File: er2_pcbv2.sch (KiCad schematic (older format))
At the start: 39 parts, among them J1 HMC5883L, J2 SPI1, J3 raspberry_b_plus_header, J4 Power, U1 MPU-6050, U2 LM2596S-5, U3 STM32F030K6Tx, Y1 8Mhz

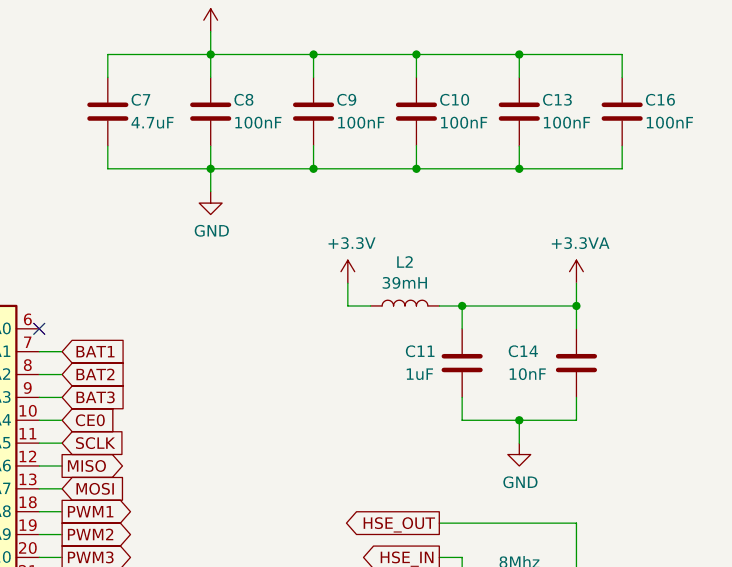
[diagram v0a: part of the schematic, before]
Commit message: packages of PCB components was assigned
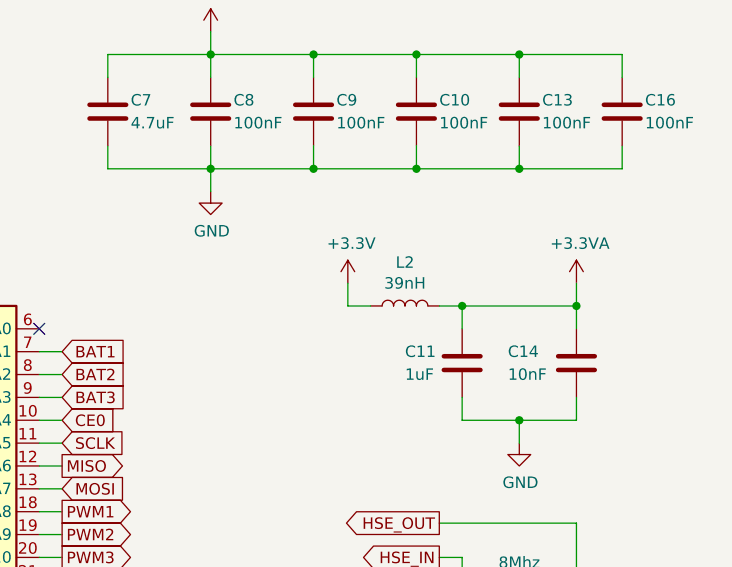
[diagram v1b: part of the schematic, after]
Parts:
- C1, C10, C11, C12, C13, C14, C15, C16, C2, C3, C4, C7, C8, C9: footprint (none) -> Capacitor_SMD:C_0805_2012Metric_Pad1.18x1.45mm_HandSolder
- C5: footprint (none) -> Capacitor_SMD:CP_Elec_10x10.5
- C6: footprint (none) -> Capacitor_SMD:CP_Elec_6.3x7.7
- D1, D3: footprint (none) -> LED_SMD:LED_0805_2012Metric_Pad1.15x1.40mm_HandSolder
- D2: footprint Diode_THT:D_DO-201AD_P15.24mm_Horizontal -> (none)
- J3: footprint (none) -> Connector_PinHeader_2.54mm:PinHeader_2x13_P2.54mm_Vertical
- J4: footprint (none) -> Connector_JST:JST_XH_B4B-XH-A_1x04_P2.50mm_Vertical
- L2: value 39mH -> 39nH
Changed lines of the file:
@@
 F 0 "D1" V 1139 5232 50  0000 R CNN
 F 1 "LED" V 1048 5232 50  0000 R CNN
-F 2 "" H 1100 5350 50  0001 C CNN
+F 2 "LED_SMD:LED_0805_2012Metric_Pad1.15x1.40mm_HandSolder" H 1100 5350 50  0001 C CNN
 F 3 "~" H 1100 5350 50  0001 C CNN
 	1    1100 5350
@@
 F 0 "J3" H 4550 7350 50  0000 C CNN
 F 1 "raspberry_b_plus_header" H 4800 5700 50  0000 C CNN
-F 2 "" H 4300 6450 50  0001 C CNN
+F 2 "Connector_PinHeader_2.54mm:PinHeader_2x13_P2.54mm_Vertical" H 4300 6450 50  0001 C CNN
 F 3 "" H 4300 6450 50  0001 C CNN
 	1    4350 6350
@@
 F 0 "C15" H 10715 5696 50  0000 L CNN
 F 1 "20p" H 10715 5605 50  0000 L CNN
-F 2 "" H 10638 5500 50  0001 C CNN
+F 2 "Capacitor_SMD:C_0805_2012Metric_Pad1.18x1.45mm_HandSolder" H 10638 5500 50  0001 C CNN
 F 3 "~" H 10600 5650 50  0001 C CNN
 	1    10600 5650
@@
 F 0 "C12" H 9850 5700 50  0000 L CNN
 F 1 "20p" H 9850 5600 50  0000 L CNN
-F 2 "" H 10138 5500 50  0001 C CNN
+F 2 "Capacitor_SMD:C_0805_2012Metric_Pad1.18x1.45mm_HandSolder" H 10138 5500 50  0001 C CNN
 F 3 "~" H 10100 5650 50  0001 C CNN
 	1    10100 5650
@@
 F 0 "C1" H 2915 3946 50  0000 L CNN
 F 1 "0.1uF" H 2915 3855 50  0000 L CNN
-F 2 "" H 2838 3750 50  0001 C CNN
+F 2 "Capacitor_SMD:C_0805_2012Metric_Pad1.18x1.45mm_HandSolder" H 2838 3750 50  0001 C CNN
 F 3 "~" H 2800 3900 50  0001 C CNN
 	1    2800 3900
@@
 F 0 "C2" H 3415 3946 50  0000 L CNN
 F 1 "2.2nF" H 3415 3855 50  0000 L CNN
-F 2 "" H 3338 3750 50  0001 C CNN
+F 2 "Capacitor_SMD:C_0805_2012Metric_Pad1.18x1.45mm_HandSolder" H 3338 3750 50  0001 C CNN
 F 3 "~" H 3300 3900 50  0001 C CNN
 	1    3300 3900
@@
 F 0 "C3" H 4100 3450 50  0000 L CNN
 F 1 "10nF" H 4100 3350 50  0000 L CNN
-F 2 "" H 4488 3250 50  0001 C CNN
+F 2 "Capacitor_SMD:C_0805_2012Metric_Pad1.18x1.45mm_HandSolder" H 4488 3250 50  0001 C CNN
 F 3 "~" H 4450 3400 50  0001 C CNN
 	1    4450 3400
@@
 F 0 "C4" H 4915 3446 50  0000 L CNN
 F 1 "0.1uF" H 4915 3355 50  0000 L CNN
-F 2 "" H 4838 3250 50  0001 C CNN
+F 2 "Capacitor_SMD:C_0805_2012Metric_Pad1.18x1.45mm_HandSolder" H 4838 3250 50  0001 C CNN
 F 3 "~" H 4800 3400 50  0001 C CNN
 	1    4800 3400
@@
 F 0 "C11" H 9850 4400 50  0000 L CNN
 F 1 "1uF" H 9850 4300 50  0000 L CNN
-F 2 "" H 10138 4200 50  0001 C CNN
+F 2 "Capacitor_SMD:C_0805_2012Metric_Pad1.18x1.45mm_HandSolder" H 10138 4200 50  0001 C CNN
 F 3 "~" H 10100 4350 50  0001 C CNN
 	1    10100 4350
@@
 F 0 "C14" H 10300 4400 50  0000 L CNN
 F 1 "10nF" H 10300 4300 50  0000 L CNN
-F 2 "" H 10638 4200 50  0001 C CNN
+F 2 "Capacitor_SMD:C_0805_2012Metric_Pad1.18x1.45mm_HandSolder" H 10638 4200 50  0001 C CNN
 F 3 "~" H 10600 4350 50  0001 C CNN
 	1    10600 4350
@@
 P 9850 4100
 F 0 "L2" V 10040 4100 50  0000 C CNN
-F 1 "39mH" V 9949 4100 50  0000 C CNN
+F 1 "39nH" V 9949 4100 50  0000 C CNN
 F 2 "" H 9850 4100 50  0001 C CNN
 F 3 "~" H 9850 4100 50  0001 C CNN
@@
 F 0 "C9" H 9550 3300 50  0000 L CNN
 F 1 "100nF" H 9550 3200 50  0000 L CNN
-F 2 "" H 9488 3100 50  0001 C CNN
+F 2 "Capacitor_SMD:C_0805_2012Metric_Pad1.18x1.45mm_HandSolder" H 9488 3100 50  0001 C CNN
 F 3 "~" H 9450 3250 50  0001 C CNN
 	1    9450 3250
@@
 F 0 "C10" H 10000 3300 50  0000 L CNN
 F 1 "100nF" H 10000 3200 50  0000 L CNN
-F 2 "" H 9938 3100 50  0001 C CNN
+F 2 "Capacitor_SMD:C_0805_2012Metric_Pad1.18x1.45mm_HandSolder" H 9938 3100 50  0001 C CNN
 F 3 "~" H 9900 3250 50  0001 C CNN
 	1    9900 3250
@@
 F 0 "C13" H 10450 3300 50  0000 L CNN
 F 1 "100nF" H 10450 3200 50  0000 L CNN
-F 2 "" H 10388 3100 50  0001 C CNN
+F 2 "Capacitor_SMD:C_0805_2012Metric_Pad1.18x1.45mm_HandSolder" H 10388 3100 50  0001 C CNN
 F 3 "~" H 10350 3250 50  0001 C CNN
 	1    10350 3250
@@
 F 0 "C16" H 10900 3300 50  0000 L CNN
 F 1 "100nF" H 10900 3200 50  0000 L CNN
-F 2 "" H 10838 3100 50  0001 C CNN
+F 2 "Capacitor_SMD:C_0805_2012Metric_Pad1.18x1.45mm_HandSolder" H 10838 3100 50  0001 C CNN
 F 3 "~" H 10800 3250 50  0001 C CNN
 	1    10800 3250
@@
 F 0 "C8" H 9100 3300 50  0000 L CNN
 F 1 "100nF" H 9100 3200 50  0000 L CNN
-F 2 "" H 9038 3100 50  0001 C CNN
+F 2 "Capacitor_SMD:C_0805_2012Metric_Pad1.18x1.45mm_HandSolder" H 9038 3100 50  0001 C CNN
 F 3 "~" H 9000 3250 50  0001 C CNN
 	1    9000 3250
@@
 F 0 "C7" H 8650 3300 50  0000 L CNN
 F 1 "4.7uF" H 8650 3200 50  0000 L CNN
-F 2 "" H 8588 3100 50  0001 C CNN
+F 2 "Capacitor_SMD:C_0805_2012Metric_Pad1.18x1.45mm_HandSolder" H 8588 3100 50  0001 C CNN
 F 3 "~" H 8550 3250 50  0001 C CNN
 	1    8550 3250
@@
 F 0 "C5" H 6050 1950 50  0000 L CNN
 F 1 "680uF" H 6050 1850 50  0000 L CNN
-F 2 "" H 6438 1750 50  0001 C CNN
+F 2 "Capacitor_SMD:CP_Elec_10x10.5" H 6438 1750 50  0001 C CNN
 F 3 "~" H 6400 1900 50  0001 C CNN
 	1    6400 1900
@@
 F 0 "D2" V 7804 1980 50  0000 L CNN
 F 1 "1N5822" V 7895 1980 50  0000 L CNN
-F 2 "Diode_THT:D_DO-201AD_P15.24mm_Horizontal" H 7850 1725 50  0001 C CNN
+F 2 "" H 7850 1725 50  0001 C CNN
 F 3 "http://www.vishay.com/docs/88526/1n5820.pdf" H 7850 1900 50  0001 C CNN
 	1    7850 1900
@@
 F 0 "C6" H 8468 1946 50  0000 L CNN
 F 1 "220uF" H 8468 1855 50  0000 L CNN
-F 2 "" H 8388 1750 50  0001 C CNN
+F 2 "Capacitor_SMD:CP_Elec_6.3x7.7" H 8388 1750 50  0001 C CNN
 F 3 "~" H 8350 1900 50  0001 C CNN
 	1    8350 1900
@@
 F 0 "D3" V 8889 1382 50  0000 R CNN
 F 1 "LED" V 8798 1382 50  0000 R CNN
-F 2 "" H 8850 1500 50  0001 C CNN
+F 2 "LED_SMD:LED_0805_2012Metric_Pad1.15x1.40mm_HandSolder" H 8850 1500 50  0001 C CNN
 F 3 "~" H 8850 1500 50  0001 C CNN
 	1    8850 1500
@@
 F 0 "J4" V 10100 1050 50  0000 R CNN
 F 1 "Power" V 10200 750 50  0000 R CNN
-F 2 "" H 10100 700 50  0001 C CNN
+F 2 "Connector_JST:JST_XH_B4B-XH-A_1x04_P2.50mm_Vertical" H 10100 700 50  0001 C CNN
 F 3 "~" H 10100 700 50  0001 C CNN
 	1    10100 700

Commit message: preliminary PCB components placement
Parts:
- D2: footprint (none) -> Diode_SMD:D_SMA_Handsoldering
- J1: footprint (none) -> Connector_JST:JST_GH_BM04B-GHS-TBT_1x04-1MP_P1.25mm_Vertical
- J2: footprint (none) -> Connector_JST:JST_GH_BM05B-GHS-TBT_1x05-1MP_P1.25mm_Vertical
- L1: footprint (none) -> Inductor_SMD:L_7.3x7.3_H3.5
- L2: footprint (none) -> Inductor_SMD:L_0603_1608Metric_Pad1.05x0.95mm_HandSolder
- R1, R10, R2, R3, R4, R5, R6, R7, R8, R9: footprint (none) -> Resistor_SMD:R_0805_2012Metric_Pad1.20x1.40mm_HandSolder
- Y1: footprint (none) -> Crystal:Crystal_SMD_HC49-SD_HandSoldering
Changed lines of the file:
@@
 F 0 "R2" H 1170 5796 50  0000 L CNN
 F 1 "1k" H 1170 5705 50  0000 L CNN
-F 2 "" V 1030 5750 50  0001 C CNN
+F 2 "Resistor_SMD:R_0805_2012Metric_Pad1.20x1.40mm_HandSolder" V 1030 5750 50  0001 C CNN
 F 3 "~" H 1100 5750 50  0001 C CNN
 	1    1100 5750
@@
 F 0 "J2" H 1900 7417 50  0000 C CNN
 F 1 "SPI1" H 1900 7326 50  0000 C CNN
-F 2 "" H 1850 7100 50  0001 C CNN
+F 2 "Connector_JST:JST_GH_BM05B-GHS-TBT_1x05-1MP_P1.25mm_Vertical" H 1850 7100 50  0001 C CNN
 F 3 "~" H 1850 7100 50  0001 C CNN
 	1    1850 7100
@@
 F 0 "Y1" H 10350 5250 50  0000 C CNN
 F 1 "8Mhz" H 10350 5577 50  0000 C CNN
-F 2 "" H 10350 5400 50  0001 C CNN
+F 2 "Crystal:Crystal_SMD_HC49-SD_HandSoldering" H 10350 5400 50  0001 C CNN
 F 3 "~" H 10350 5400 50  0001 C CNN
 	1    10350 5400
@@
 F 0 "R3" V 2100 5950 50  0000 C CNN
 F 1 "4.7k" V 2300 5950 50  0000 C CNN
-F 2 "" V 2130 5950 50  0001 C CNN
+F 2 "Resistor_SMD:R_0805_2012Metric_Pad1.20x1.40mm_HandSolder" V 2130 5950 50  0001 C CNN
 F 3 "~" H 2200 5950 50  0001 C CNN
 	1    2200 5950
@@
 F 0 "R4" V 2100 6250 50  0000 C CNN
 F 1 "4.7k" V 2300 6250 50  0000 C CNN
-F 2 "" V 2130 6250 50  0001 C CNN
+F 2 "Resistor_SMD:R_0805_2012Metric_Pad1.20x1.40mm_HandSolder" V 2130 6250 50  0001 C CNN
 F 3 "~" H 2200 6250 50  0001 C CNN
 	1    2200 6250
@@
 F 0 "J1" V 1800 850 50  0000 R CNN
 F 1 "HMC5883L" V 1900 1300 50  0000 R CNN
-F 2 "" H 1800 1150 50  0001 C CNN
+F 2 "Connector_JST:JST_GH_BM04B-GHS-TBT_1x04-1MP_P1.25mm_Vertical" H 1800 1150 50  0001 C CNN
 F 3 "~" H 1800 1150 50  0001 C CNN
 	1    1800 1150
@@
 F 0 "R1" V 850 3500 50  0000 C CNN
 F 1 "1k" V 1050 3500 50  0000 C CNN
-F 2 "" V 880 3500 50  0001 C CNN
+F 2 "Resistor_SMD:R_0805_2012Metric_Pad1.20x1.40mm_HandSolder" V 880 3500 50  0001 C CNN
 F 3 "~" H 950 3500 50  0001 C CNN
 	1    950  3500
@@
 F 0 "L2" V 10040 4100 50  0000 C CNN
 F 1 "39nH" V 9949 4100 50  0000 C CNN
-F 2 "" H 9850 4100 50  0001 C CNN
+F 2 "Inductor_SMD:L_0603_1608Metric_Pad1.05x0.95mm_HandSolder" H 9850 4100 50  0001 C CNN
 F 3 "~" H 9850 4100 50  0001 C CNN
 	1    9850 4100
@@
 F 0 "L1" V 8200 1650 50  0000 C CNN
 F 1 "33uH" V 8050 1650 50  0000 C CNN
-F 2 "" H 8100 1650 50  0001 C CNN
+F 2 "Inductor_SMD:L_7.3x7.3_H3.5" H 8100 1650 50  0001 C CNN
 F 3 "~" H 8100 1650 50  0001 C CNN
 	1    8100 1650
@@
 F 0 "D2" V 7804 1980 50  0000 L CNN
 F 1 "1N5822" V 7895 1980 50  0000 L CNN
-F 2 "" H 7850 1725 50  0001 C CNN
+F 2 "Diode_SMD:D_SMA_Handsoldering" H 7850 1725 50  0001 C CNN
 F 3 "http://www.vishay.com/docs/88526/1n5820.pdf" H 7850 1900 50  0001 C CNN
 	1    7850 1900
@@
 F 0 "R5" H 8920 1946 50  0000 L CNN
 F 1 "1k" H 8920 1855 50  0000 L CNN
-F 2 "" V 8780 1900 50  0001 C CNN
+F 2 "Resistor_SMD:R_0805_2012Metric_Pad1.20x1.40mm_HandSolder" V 8780 1900 50  0001 C CNN
 F 3 "~" H 8850 1900 50  0001 C CNN
 	1    8850 1900
@@
 F 0 "R6" H 10050 1600 50  0000 C CNN
 F 1 "22k" H 10050 1500 50  0000 C CNN
-F 2 "" V 9830 1550 50  0001 C CNN
+F 2 "Resistor_SMD:R_0805_2012Metric_Pad1.20x1.40mm_HandSolder" V 9830 1550 50  0001 C CNN
 F 3 "~" H 9900 1550 50  0001 C CNN
 	1    9900 1550
@@
 F 0 "R7" H 10470 1596 50  0000 L CNN
 F 1 "10k" H 10470 1505 50  0000 L CNN
-F 2 "" V 10330 1550 50  0001 C CNN
+F 2 "Resistor_SMD:R_0805_2012Metric_Pad1.20x1.40mm_HandSolder" V 10330 1550 50  0001 C CNN
 F 3 "~" H 10400 1550 50  0001 C CNN
 	1    10400 1550
@@
 F 0 "R8" H 10470 1996 50  0000 L CNN
 F 1 "10k" H 10470 1905 50  0000 L CNN
-F 2 "" V 10330 1950 50  0001 C CNN
+F 2 "Resistor_SMD:R_0805_2012Metric_Pad1.20x1.40mm_HandSolder" V 10330 1950 50  0001 C CNN
 F 3 "~" H 10400 1950 50  0001 C CNN
 	1    10400 1950
@@
 F 0 "R9" H 10970 1596 50  0000 L CNN
 F 1 "22k" H 10970 1505 50  0000 L CNN
-F 2 "" V 10830 1550 50  0001 C CNN
+F 2 "Resistor_SMD:R_0805_2012Metric_Pad1.20x1.40mm_HandSolder" V 10830 1550 50  0001 C CNN
 F 3 "~" H 10900 1550 50  0001 C CNN
 	1    10900 1550
@@
 F 0 "R10" H 10970 1996 50  0000 L CNN
 F 1 "10k" H 10970 1905 50  0000 L CNN
-F 2 "" V 10830 1950 50  0001 C CNN
+F 2 "Resistor_SMD:R_0805_2012Metric_Pad1.20x1.40mm_HandSolder" V 10830 1950 50  0001 C CNN
 F 3 "~" H 10900 1950 50  0001 C CNN
 	1    10900 1950
